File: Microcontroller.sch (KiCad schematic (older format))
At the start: 19 parts

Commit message: Finished Emergency Circuit
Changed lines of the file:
@@
 $Descr A4 11693 8268
 encoding utf-8
-Sheet 4 6
+Sheet 4 9
 Title "Microcontroller"
 Date "2019-12-19"
@@
 	1    0    0    -1
 $EndComp
+Text GLabel 7050 3050 0    50   Input ~ 0
+Y_ENABLE
+Text GLabel 7050 3200 0    50   Input ~ 0
+Z_ENABLE
+Text GLabel 6650 3350 2    50   Output ~ 0
+EMERGENCY
 $EndSCHEMATC

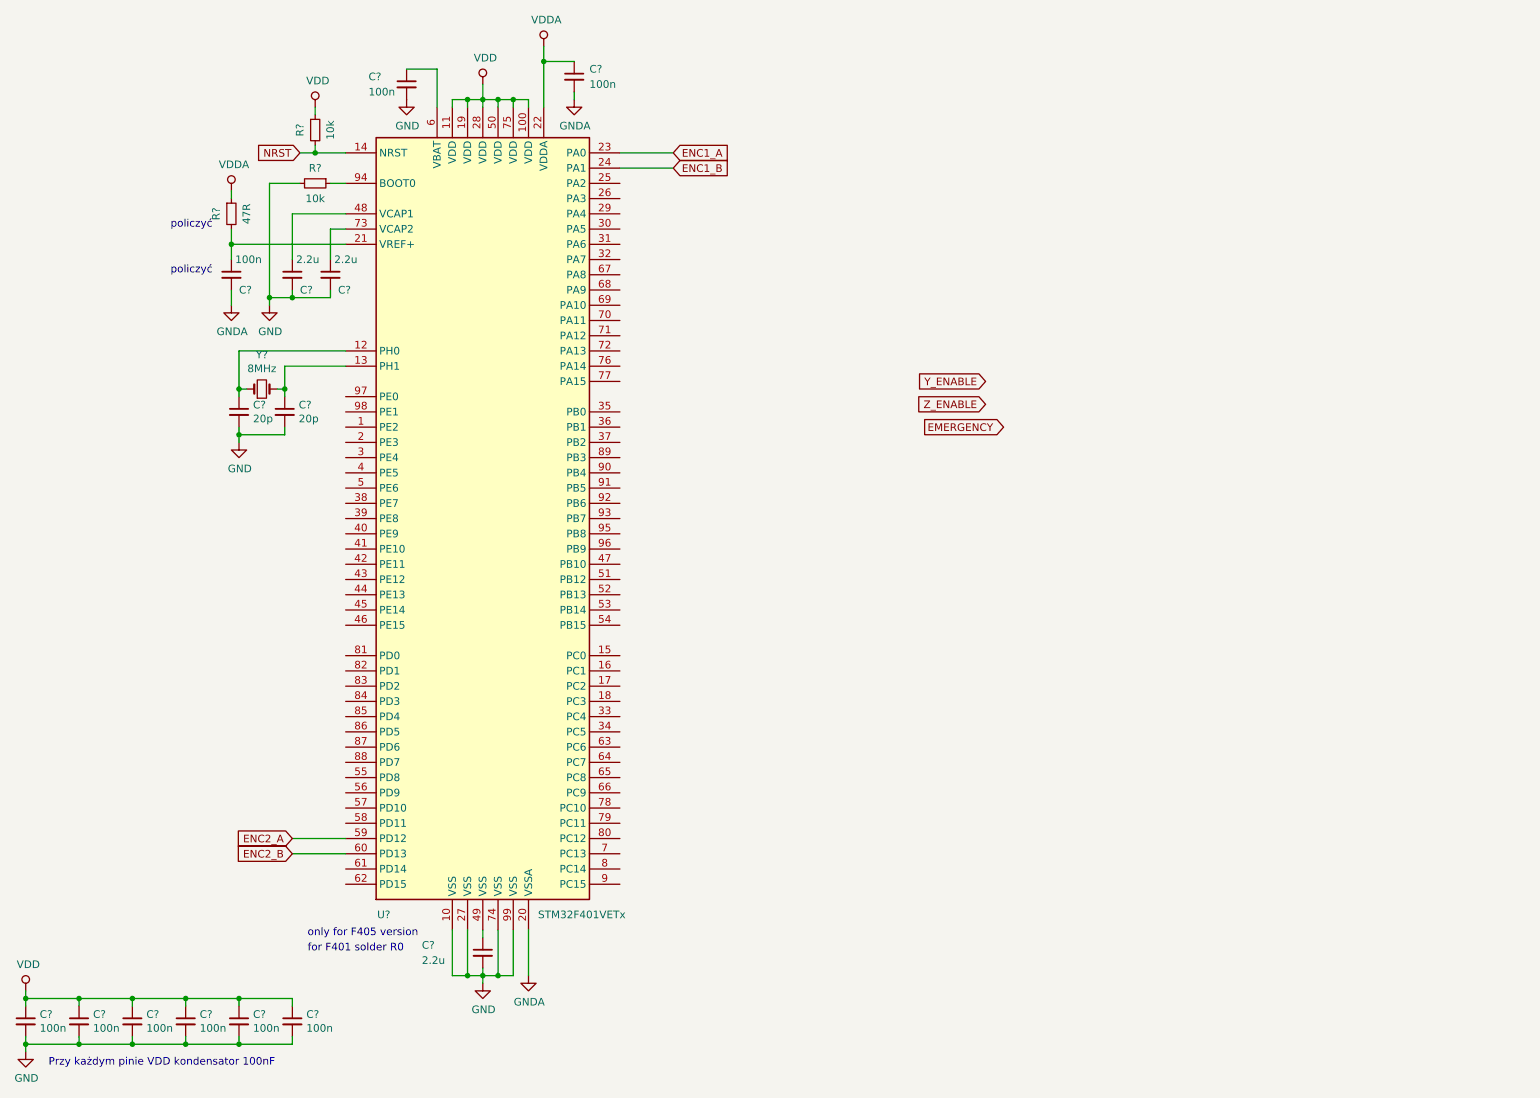
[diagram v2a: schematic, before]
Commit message: Added USB B socket with ESD filter
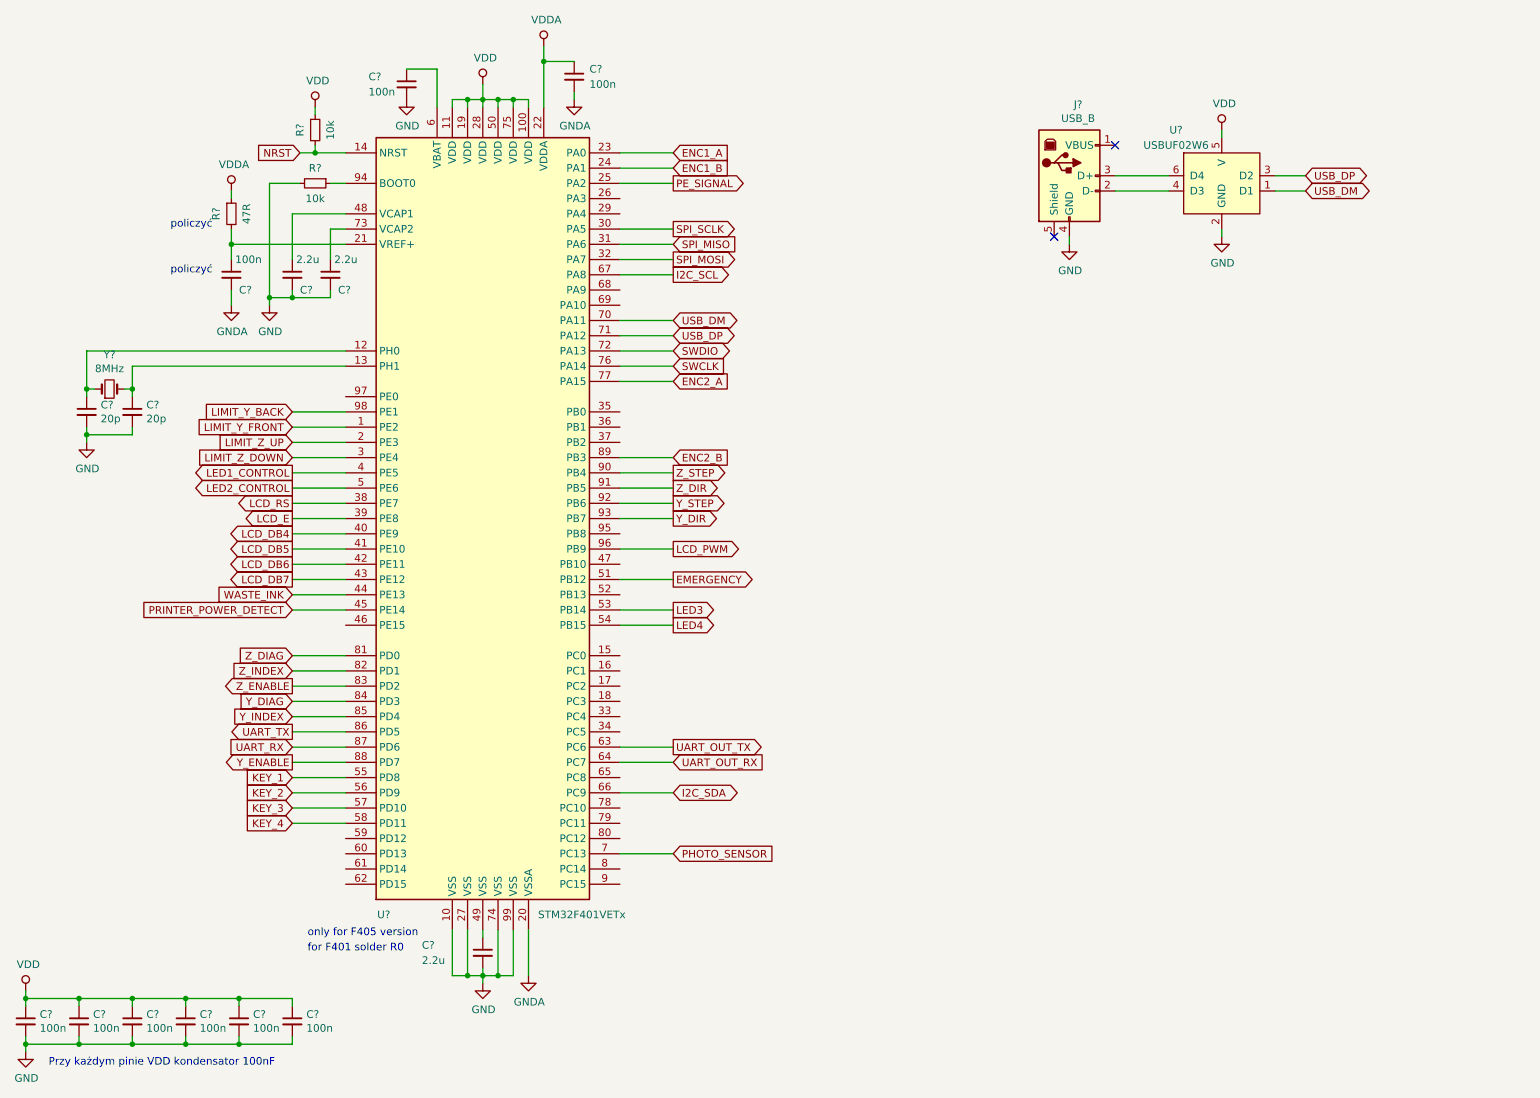
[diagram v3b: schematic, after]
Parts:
- added J?: USB_B, Connector_USB:USB_B_OST_USB-B1HSxx_Horizontal, symbol Connector:USB_B
- added U?: USBUF02W6, symbol Library:USBUF02W6
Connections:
- net EMERGENCY: now also U?.51 (PB12)
- net ENC2_A: now also U?.77 (PA15); no longer U?.59 (PD12)
- net ENC2_B: now also U?.89 (PB3); no longer U?.60 (PD13)
- net GND: now also J?.4 (GND), U?.2 (GND)
- net VDD: now also U?.5 (V)
- net Y_ENABLE: now also U?.88 (PD7)
- net Z_ENABLE: now also U?.83 (PD2)
- net LIMIT_Y_FRONT: now reaches U?.1 (PE2)
- net LIMIT_Z_UP: now reaches U?.2 (PE3)
- net PE_SIGNAL: now reaches U?.25 (PA2)
- net LIMIT_Z_DOWN: now reaches U?.3 (PE4)
- net SPI_SCLK: now reaches U?.30 (PA5)
- net SPI_MISO: now reaches U?.31 (PA6)
- net SPI_MOSI: now reaches U?.32 (PA7)
- net LCD_RS: now reaches U?.38 (PE7)
- net LCD_E: now reaches U?.39 (PE8)
- net LED1_CONTROL: now reaches U?.4 (PE5)
- net LCD_DB4: now reaches U?.40 (PE9)
- net LCD_DB5: now reaches U?.41 (PE10)
- net LCD_DB6: now reaches U?.42 (PE11)
- net LCD_DB7: now reaches U?.43 (PE12)
- net WASTE_INK: now reaches U?.44 (PE13)
- net PRINTER_POWER_DETECT: now reaches U?.45 (PE14)
- net LED2_CONTROL: now reaches U?.5 (PE6)
- net LED3: now reaches U?.53 (PB14)
- net LED4: now reaches U?.54 (PB15)
- net KEY_1: now reaches U?.55 (PD8)
- net KEY_2: now reaches U?.56 (PD9)
- net KEY_3: now reaches U?.57 (PD10)
- net KEY_4: now reaches U?.58 (PD11)
- net UART_OUT_TX: now reaches U?.63 (PC6)
- net UART_OUT_RX: now reaches U?.64 (PC7)
- net I2C_SDA: now reaches U?.66 (PC9)
- net I2C_SCL: now reaches U?.67 (PA8)
- net PHOTO_SENSOR: now reaches U?.7 (PC13)
- net USB_DM: now reaches U?.70 (PA11)
- net USB_DM: now also U?.1 (D1)
- net USB_DP: now reaches U?.71 (PA12)
- net USB_DP: now also U?.3 (D2)
- net SWDIO: now reaches U?.72 (PA13)
- net SWCLK: now reaches U?.76 (PA14)
- net Z_DIAG: now reaches U?.81 (PD0)
- net Z_INDEX: now reaches U?.82 (PD1)
- net Y_DIAG: now reaches U?.84 (PD3)
- net Y_INDEX: now reaches U?.85 (PD4)
- net UART_TX: now reaches U?.86 (PD5)
- net UART_RX: now reaches U?.87 (PD6)
- net Z_STEP: now reaches U?.90 (PB4)
- net Z_DIR: now reaches U?.91 (PB5)
- net Y_STEP: now reaches U?.92 (PB6)
- net Y_DIR: now reaches U?.93 (PB7)
- net LCD_PWM: now reaches U?.96 (PB9)
- net LIMIT_Y_BACK: now reaches U?.98 (PE1)
- new net: J?.2 (D-), U?.4 (D3)
- new net: J?.3 (D+), U?.6 (D4)
- no-connect marks 0 -> 2
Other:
- moved on the sheet: C?, Y?

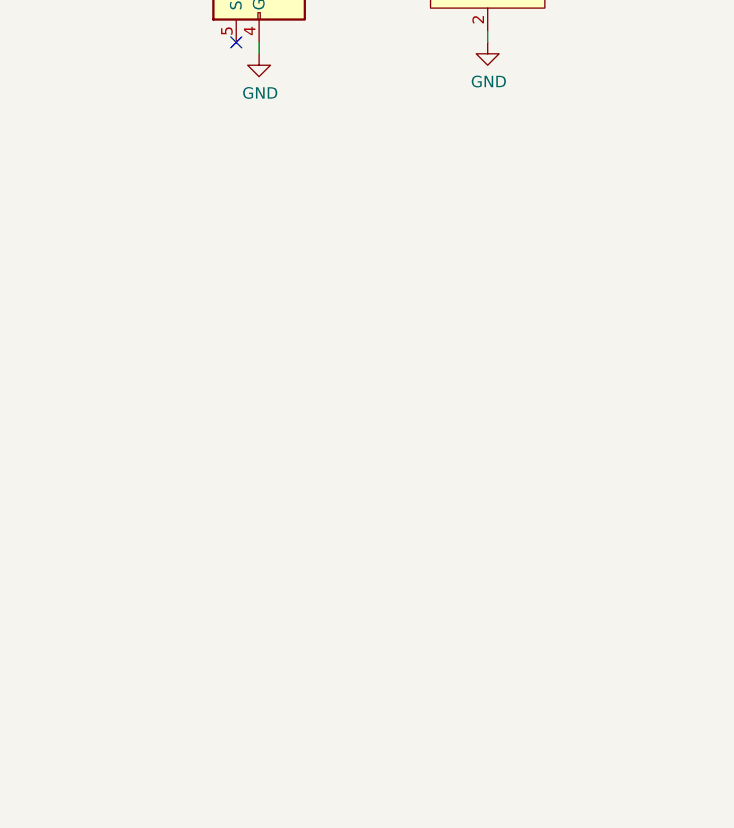
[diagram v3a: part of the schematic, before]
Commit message: Added SWD and Debug out
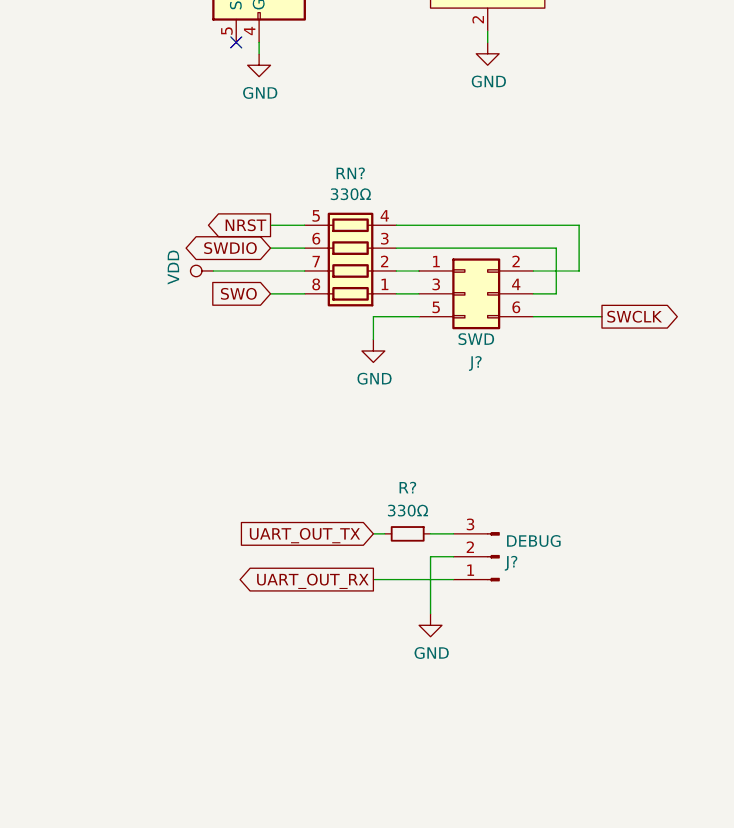
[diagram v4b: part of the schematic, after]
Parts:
- added J?: SWD, Connector_IDC:IDC-Header_2x03_P2.54mm_Vertical, symbol Connector_Generic:Conn_02x03_Odd_Even
- added J?: DEBUG, Connector_JST:JST_PH_B2B-PH-K_1x03_P2.00mm_Vertical, symbol Connector:Conn_01x03_Male
- added R?: 330Ω, symbol Device:R_Small
- added RN?: 330Ω, Resistor_SMD:R_Array_Concave_4x0603, symbol Device:R_Pack04
- U?: footprint (none) -> footprints:SOT323-6L
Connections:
- net GND: now also J?.2 (Pin_2), J?.5 (Pin_5)
- net NRST: now also RN?.5 (R4.2)
- net SWCLK: now also J?.6 (Pin_6)
- net SWDIO: now also RN?.6 (R3.2)
- net UART_OUT_RX: now also J?.1 (Pin_1)
- net UART_OUT_TX: now also R?.2
- net VDD: now also RN?.7 (R2.2)
- new net: J?.1 (Pin_1), RN?.2 (R2.1)
- new net: J?.2 (Pin_2), RN?.4 (R4.1)
- new net: J?.3 (Pin_3), RN?.1 (R1.1)
- new net: J?.4 (Pin_4), RN?.3 (R3.1)
- new net: J?.3 (Pin_3), R?.1
- new net SWO: RN?.8 (R1.2)
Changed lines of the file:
@@
 F 0 "U?" H 8300 2100 50  0000 C CNN
 F 1 "USBUF02W6" H 8300 2000 50  0000 C CNN
-F 2 "" H 9250 2400 50  0001 C CNN
+F 2 "footprints:SOT323-6L" H 9250 2400 50  0001 C CNN
 F 3 "" H 9250 2400 50  0001 C CNN
 	1    8600 1750
@@
 Wire Wire Line
 	7900 1800 8250 1800
+$Comp
+L Connector_Generic:Conn_02x03_Odd_Even J?
+U 1 1 5E16DD76
+P 8500 3200
+F 0 "J?" H 8550 2900 50  0000 C CNN
+F 1 "SWD" H 8550 3000 50  0000 C CNN
+F 2 "Connector_IDC:IDC-Header_2x03_P2.54mm_Vertical" H 8500 3200 50  0001 C CNN
+F 3 "~" H 8500 3200 50  0001 C CNN
+	1    8500 3200
+	1    0    0    -1
+$EndComp
+$Comp
+L power:VDD #PWR?
+U 1 1 5E17BC07
+P 7400 3100
+F 0 "#PWR?" H 7400 2950 50  0001 C CNN
+F 1 "VDD" H 7417 3273 50  0000 C CNN
+F 2 "" H 7400 3100 50  0001 C CNN
+F 3 "" H 7400 3100 50  0001 C CNN
+	1    7400 3100
+	0    -1   -1   0
+$EndComp
+Wire Wire Line
+	7800 3100 7400 3100
+Text GLabel 7650 2900 0    50   Output ~ 0
+NRST
+Wire Wire Line
+	8800 3100 9000 3100
+Text GLabel 7650 3200 0    50   Input ~ 0
+SWO
+Wire Wire Line
+	7650 3200 7800 3200
+Text GLabel 7650 3000 0    50   BiDi ~ 0
+SWDIO
+$Comp
+L power:GND #PWR?
+U 1 1 5E1C4BF1
+P 8350 4600
+F 0 "#PWR?" H 8350 4350 50  0001 C CNN
+F 1 "GND" H 8355 4427 50  0000 C CNN
+F 2 "" H 8350 4600 50  0001 C CNN
+F 3 "" H 8350 4600 50  0001 C CNN
+	1    8350 4600
+	1    0    0    -1
+$EndComp
+Wire Wire Line
+	8800 3300 9100 3300
+Wire Wire Line
+	8300 3300 8100 3300
+Wire Wire Line
+	8100 3300 8100 3400
+$Comp
+L Device:R_Pack04 RN?
+U 1 1 5E27A122
+P 8000 3000
+AR Path="/5E07245F/5E27A122" Ref="RN?"  Part="1"
+AR Path="/5E858220/5E27A122" Ref="RN?"  Part="1"
+AR Path="/5DFB2EC0/5E27A122" Ref="RN?"  Part="1"
+F 0 "RN?" V 8325 3000 50  0000 C CNN
+F 1 "330Ω" V 8234 3000 50  0000 C CNN
+F 2 "Resistor_SMD:R_Array_Concave_4x0603" V 8275 3000 50  0001 C CNN
+F 3 "~" H 8000 3000 50  0001 C CNN
+	1    8000 3000
+	0    -1   -1   0
+$EndComp
+Wire Wire Line
+	8800 3200 8900 3200
+Wire Wire Line
+	8200 3200 8300 3200
+Wire Wire Line
+	8200 3100 8300 3100
+Wire Wire Line
+	8200 3000 8900 3000
+Wire Wire Line
+	8900 3000 8900 3200
+Wire Wire Line
+	7800 3000 7650 3000
+Wire Wire Line
+	8200 2900 9000 2900
+Wire Wire Line
+	9000 2900 9000 3100
+Wire Wire Line
+	7800 2900 7650 2900
+$Comp
+L Connector:Conn_01x03_Male J?
+U 1 1 5E3B0D8E
+P 8650 4350
+AR Path="/5E07245F/5E3B0D8E" Ref="J?"  Part="1"
+AR Path="/5E858220/5E3B0D8E" Ref="J?"  Part="1"
+AR Path="/5E91D96F/5E3B0D8E" Ref="J?"  Part="1"
+AR Path="/5DFB2EC0/5E3B0D8E" Ref="J?"  Part="1"
+F 0 "J?" H 8622 4374 50  0000 R CNN
+F 1 "DEBUG" H 8622 4283 50  0000 R CNN
+F 2 "Connector_JST:JST_PH_B2B-PH-K_1x03_P2.00mm_Vertical" H 8650 4350 50  0001 C CNN
+F 3 "~" H 8650 4350 50  0001 C CNN
+	1    8650 4350
+	-1   0    0    1
+$EndComp
+Text GLabel 8100 4250 0    50   Input ~ 0
+UART_OUT_TX
+Text GLabel 8100 4450 0    50   Output ~ 0
+UART_OUT_RX
+Wire Wire Line
+	8450 4450 8100 4450
+Wire Wire Line
+	8450 4350 8350 4350
+Wire Wire Line
+	8350 4350 8350 4600
+$Comp
+L power:GND #PWR?
+U 1 1 5E3E776E
+P 8100 3400
+F 0 "#PWR?" H 8100 3150 50  0001 C CNN
+F 1 "GND" H 8105 3227 50  0000 C CNN
+F 2 "" H 8100 3400 50  0001 C CNN
+F 3 "" H 8100 3400 50  0001 C CNN
+	1    8100 3400
+	1    0    0    -1
+$EndComp
+$Comp
+L Device:R_Small R?
+U 1 1 5E3F628C
+P 8250 4250
+F 0 "R?" V 8050 4250 50  0000 C CNN
+F 1 "330Ω" V 8150 4250 50  0000 C CNN
+F 2 "" H 8250 4250 50  0001 C CNN
+F 3 "~" H 8250 4250 50  0001 C CNN
+	1    8250 4250
+	0    1    1    0
+$EndComp
+Wire Wire Line
+	8100 4250 8150 4250
+Wire Wire Line
+	8350 4250 8450 4250
+Text GLabel 9100 3300 2    50   Output ~ 0
+SWCLK
 $EndSCHEMATC

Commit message: Improve schematics add new elements
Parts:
- removed R?: 330Ω, symbol Device:R_Small
- removed RN?: 330Ω, Resistor_SMD:R_Array_Concave_4x0603, symbol Device:R_Pack04
- added D?: OF-SMD2012G-1, Diode_SMD:D_0805_2012Metric, symbol Device:LED_ALT
- added FB?: 1000@100MHz, Inductor_SMD:L_0805_2012Metric, symbol Device:Ferrite_Bead_Small
- added R? (x2): 330Ω, symbol Device:R
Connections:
- net NRST: now also J?.2 (Pin_2)
- net SWDIO: now also J?.4 (Pin_4)
- net SWO: now also J?.3 (Pin_3)
- net UART_OUT_TX: now also J?.3 (Pin_3)
- net VDD: now also FB?.1, R?.2
- net LED_STATUS: now reaches U?.15 (PC0)
- net LED_STATUS: now also D?.1 (K)
- net TABLE_SENSOR: now reaches U?.46 (PE15)
- net at J?.1 (Pin_1): now also R?.1
- new net: D?.2 (A), R?.2
- new net +3V3: FB?.2, R?.1
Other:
- moved on the sheet: C?

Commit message: Numbering and finishing the schematic
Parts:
- added C30: 1uF, symbol Device:C_Small
- added FB9: 1000@100MHz, Inductor_SMD:L_0805_2012Metric, symbol Device:Ferrite_Bead_Small
- added Q1: BC817, Package_TO_SOT_SMD:SOT-23, symbol Transistor_BJT:BC817
- added R14, R15: 10kΩ, symbol Device:R
- C29, C31, C32, C37, C38, C39, C40, C41, C42: renamed from C?; value 100n -> 0.1uF
- C33, C34: renamed from C?; value 2.2u -> 2.2uF
- C35, C36: renamed from C?; value 20p -> 20pF
- R10, R11: renamed from R?; value 10k -> 10kΩ
- R12: renamed from R?; value 47R -> 47RΩ
- R17: renamed from C?; value 2.2u -> 0Ω; symbol Device:C_Small -> Device:R_Small
- gave numbers to parts that had none: 10
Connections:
- net ENC2_B is gone; now on net SWO: U4.89 (PB3)
- net GNDA is gone; now on net GND: C29.2, C32.2, U4.20 (VSSA)
- net +3V3: now also FB9.2, R14.2
- net GND: now also C30.2, Q1.2 (E)
- net VDD: now also C31.1, U4.6 (VBAT)
- net VDDA: now also C30.1, FB9.1
- net at U4.61 (PD14): now also Q1.3 (C), R14.1
- net ENC2_A: no longer names the net of U4.77 (PA15)
- new net: Q1.1 (B), R15.2
- new net +5V: R15.1
- no-connect marks 2 -> 28
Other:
- note added: "ENC2_A"
- note added: "ENC2_B"
- note added: "for F401 solder resistor 0Ω"
- note added: "for F405 version solder 2.2uF\n"
- note added: "sprawdzić VBAT"
- note removed: "for F401 solder R0"
- note removed: "only for F405 version\n"
- moved on the sheet: D17, R16
